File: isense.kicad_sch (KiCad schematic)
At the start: 28 parts, among them U1 MAX4073T, U2 OPA551U, U3 TLV9301xDBV, U4 OPA551U, U5 TLV9301xDBV

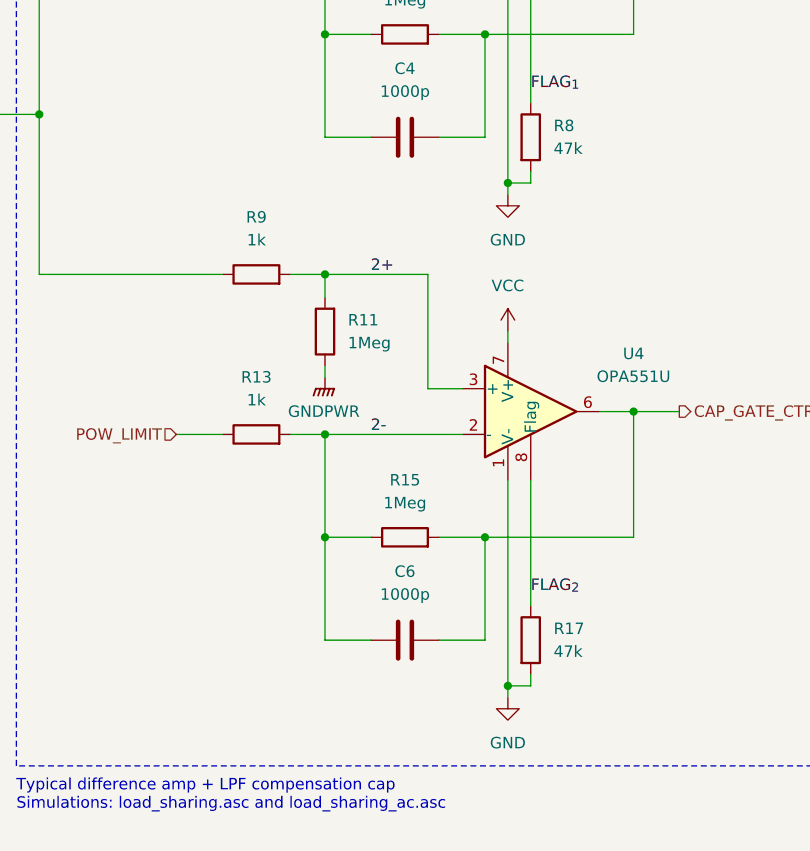
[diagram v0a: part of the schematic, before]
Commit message: Add voltage ratings to capacitors & respec caps to not explode
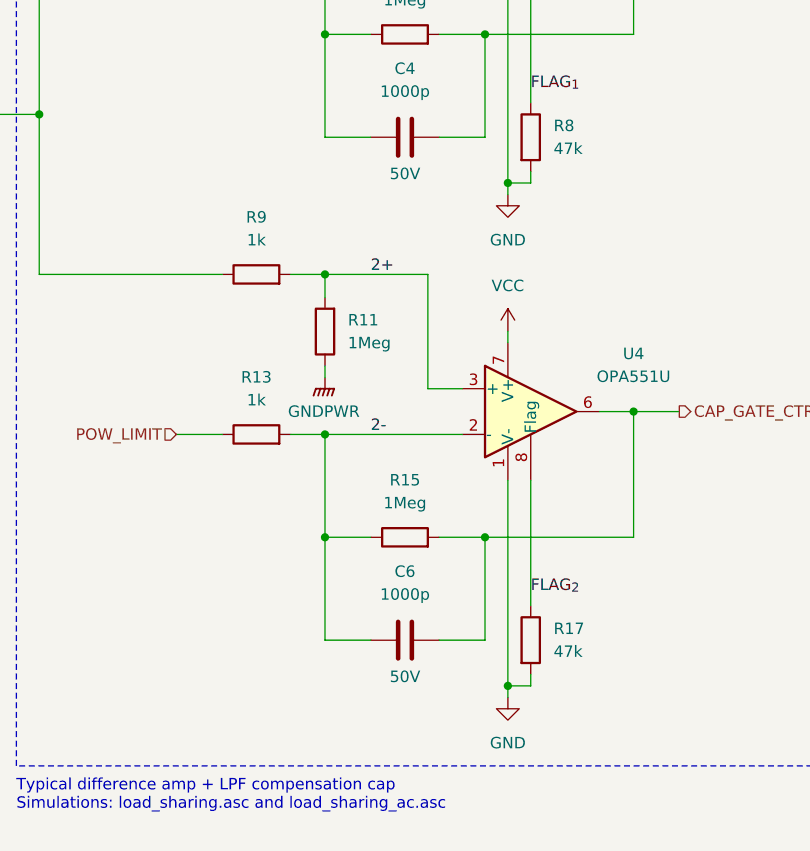
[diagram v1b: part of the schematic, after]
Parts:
- C4, C6: Voltage Rating (none) -> 50V
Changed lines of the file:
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@@
 		(on_board yes)
 		(dnp no)
-		(fields_autoplaced yes)
 		(property "Reference" "C6"
 			(at 232.41 123.19 90)
@@
 		(property "Mouser Price/Stock" ""
 			(at 232.41 130.81 0)
+			(effects
+				(font
+					(size 1.27 1.27)
+				)
+			)
+		)
+		(property "Voltage Rating" "50V"
+			(at 232.41 134.874 90)
 			(effects
 				(font
@@
 		(on_board yes)
 		(dnp no)
-		(fields_autoplaced yes)
 		(property "Reference" "C4"
 			(at 232.41 67.31 90)
@@
 			(effects
 				(font
+					(size 1.27 1.27)
+				)
+			)
+		)
+		(property "Voltage Rating" "50V"
+			(at 232.41 78.994 90)
+			(effects
+				(font

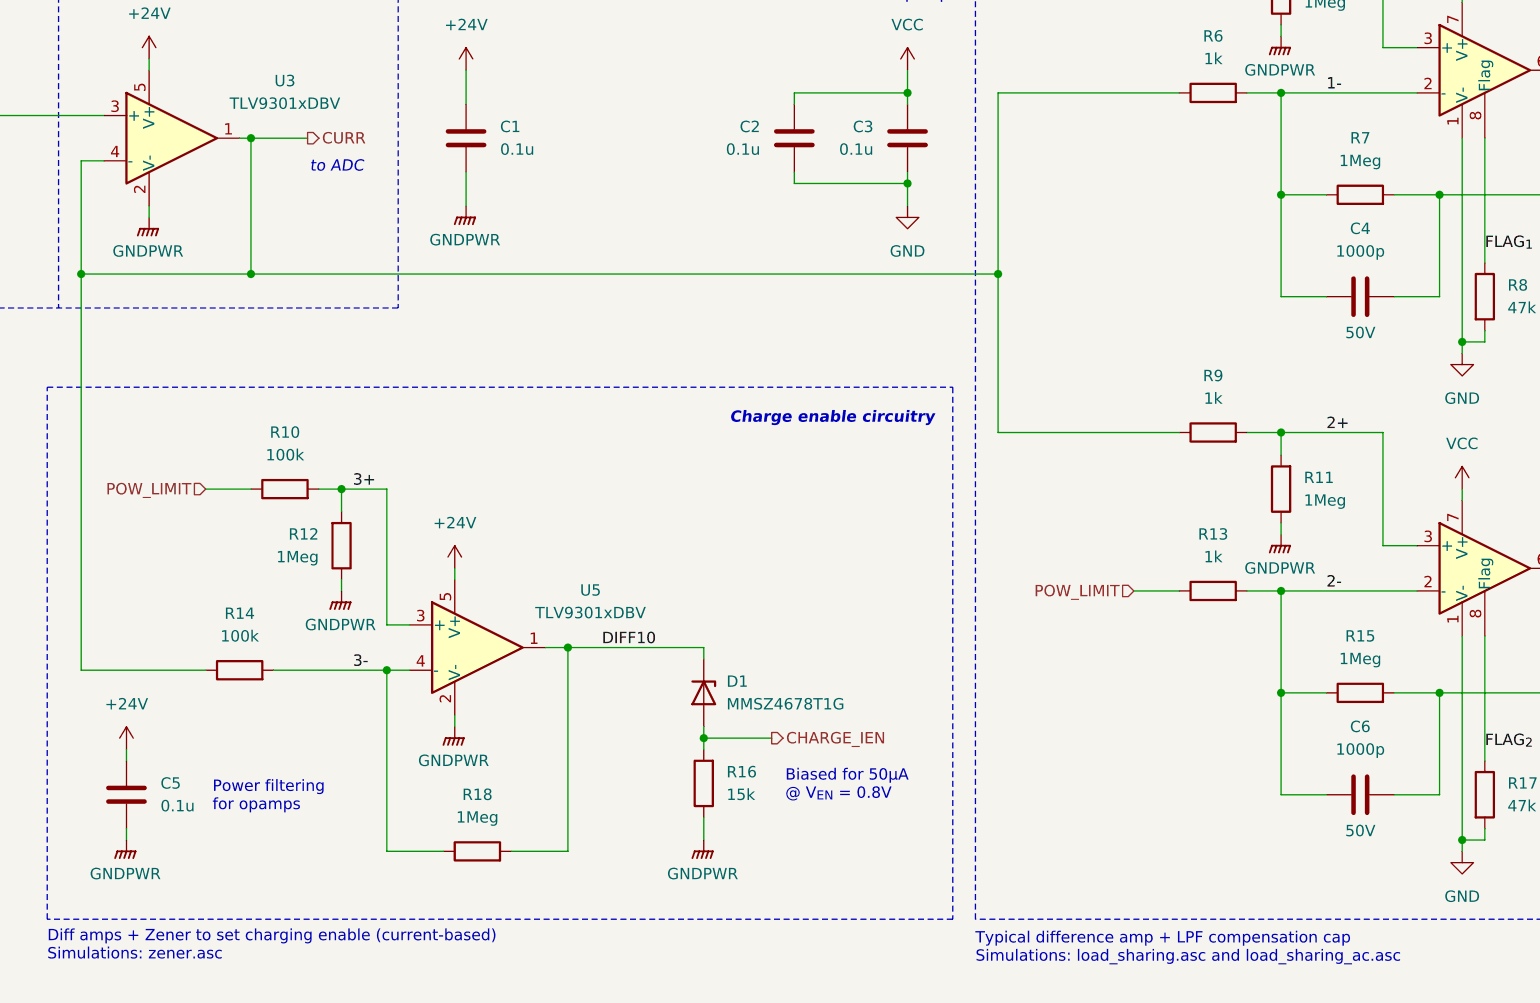
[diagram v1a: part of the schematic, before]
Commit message: Specc'd all components + started creating rev 1b boards
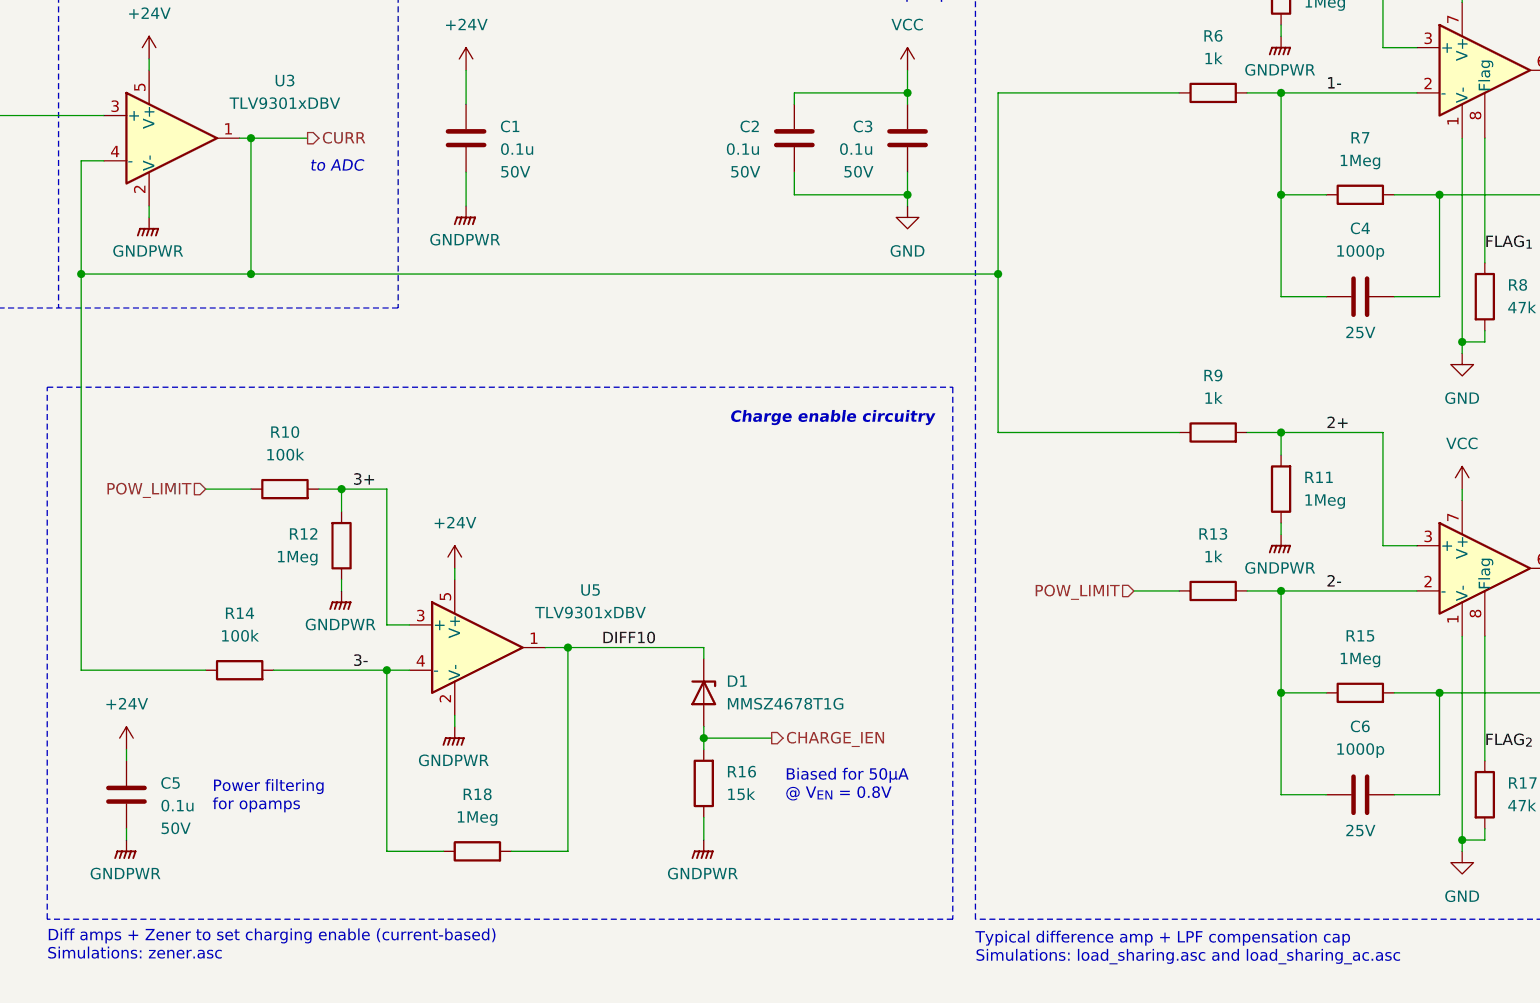
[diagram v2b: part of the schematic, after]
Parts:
- C1, C2, C3, C5: Mouser Part Number (none) -> 581-KGM15BR71H104JT; Voltage Rating (none) -> 50V
- C4, C6: Mouser Part Number 791-0603N390F500CT -> 80-C0603C102J3G; Voltage Rating 50V -> 25V
- R10, R14: Mouser Part Number (none) -> 660-RN73H1JTD1003D25
- R11, R12, R15, R18, R5, R7: Mouser Part Number 603-RC0603FR-1010ML -> 603-RC0603FR-071MP
- R13, R4, R6, R9: Mouser Part Number 755-ESR03EZPJ222 -> 660-RN73R1JTD1001F50
- R16: Mouser Part Number 603-RC0603FR-071M05L -> 603-RT0603FRE1315KL
- R17, R8: Mouser Part Number (none) -> 603-RC0603FR-1047KL
- U1: Mouser Part Number (none) -> 700-MAX4073TAUT+T
- U2, U4: Mouser Part Number (none) -> 595-OPA551UA
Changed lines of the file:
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@@
 	)
 	(junction
-		(at 181.61 62.23)
+		(at 223.52 63.5)
 		(diameter 0)
 		(color 0 0 0 0)
 	)
 	(junction
-		(at 223.52 63.5)
+		(at 181.61 63.5)
 		(diameter 0)
 		(color 0 0 0 0)
@@
 	(wire
 		(pts
-			(xy 181.61 62.23) (xy 181.61 64.77)
+			(xy 181.61 60.96) (xy 181.61 63.5)
 		)
 		(stroke
@@
 	(wire
 		(pts
-			(xy 181.61 60.96) (xy 181.61 62.23)
-		)
-		(stroke
-			(width 0)
-			(type default)
-		)
-	)
-	(wire
-		(pts
 			(xy 107.95 57.15) (xy 106.68 57.15)
 		)
@@
 	(wire
 		(pts
-			(xy 168.91 62.23) (xy 181.61 62.23)
+			(xy 181.61 63.5) (xy 181.61 64.77)
+		)
+		(stroke
+			(width 0)
+			(type default)
+		)
+	)
+	(wire
+		(pts
+			(xy 168.91 63.5) (xy 181.61 63.5)
 		)
 		(stroke
@@
 	(wire
 		(pts
-			(xy 168.91 60.96) (xy 168.91 62.23)
+			(xy 168.91 60.96) (xy 168.91 63.5)
 		)
 		(stroke
@@
 			)
 		)
-		(property "Mouser Part Number" "603-RC0603FR-1010ML"
+		(property "Mouser Part Number" "603-RC0603FR-071MP"
 			(at 223.52 40.64 0)
 			(effects
@@
 			)
 		)
-		(property "Mouser Part Number" "603-RC0603FR-071M05L"
+		(property "Mouser Part Number" "603-RT0603FRE1315KL"
 			(at 158.75 129.54 0)
 			(effects
@@
 			)
 		)
-		(property "Mouser Part Number" "603-RC0603FR-1010ML"
+		(property "Mouser Part Number" "603-RC0603FR-071MP"
 			(at 118.11 102.87 0)
 			(effects
@@
 			)
 		)
+		(property "Mouser Part Number" "660-RN73H1JTD1003D25"
+			(at 111.76 96.52 0)
+			(effects
+				(font
+					(size 1.27 1.27)
+				)
+				(hide yes)
+			)
+		)
 		(pin "1"
 		)
@@
 			)
 		)
-		(property "Mouser Part Number" "755-ESR03EZPJ222"
+		(property "Mouser Part Number" "660-RN73R1JTD1001F50"
 			(at 215.9 52.07 0)
 			(effects
@@
 			)
 		)
+		(property "Mouser Part Number" "603-RC0603FR-1047KL"
+			(at 246.38 130.81 0)
+			(effects
+				(font
+					(size 1.27 1.27)
+				)
+				(hide yes)
+			)
+		)
 		(pin "1"
 		)
@@
 			)
 		)
+		(property "Mouser Part Number" "700-MAX4073TAUT+T"
+			(at 44.45 43.18 0)
+			(effects
+				(font
+					(size 1.27 1.27)
+				)
+				(hide yes)
+			)
+		)
 		(pin "6"
 		)
@@
 		(on_board yes)
 		(dnp no)
-		(fields_autoplaced yes)
 		(property "Reference" "C2"
 			(at 165.1 55.8799 0)
@@
 			)
 		)
-		(property "Datasheet" "~"
+		(property "Datasheet" "https://www.mouser.com/datasheet/2/40/KGM_X7R-3223212.pdf"
 			(at 168.91 57.15 0)
 			(effects
@@
 			)
 		)
+		(property "Mouser Part Number" "581-KGM15BR71H104JT"
+			(at 168.91 57.15 0)
+			(effects
+				(font
+					(size 1.27 1.27)
+				)
+				(hide yes)
+			)
+		)
+		(property "Voltage Rating" "50V"
+			(at 165.1 60.96 0)
+			(effects
+				(font
+					(size 1.27 1.27)
+				)
+				(justify left)
+			)
+		)
 		(pin "2"
 		)
@@
 			)
 		)
+		(property "Mouser Part Number" "595-OPA551UA"
+			(at 246.38 49.53 0)
+			(effects
+				(font
+					(size 1.27 1.27)
+				)
+				(hide yes)
+			)
+		)
 		(pin "1"
 		)
@@
 			)
 		)
-		(property "Mouser Part Number" "755-ESR03EZPJ222"
+		(property "Mouser Part Number" "660-RN73R1JTD1001F50"
 			(at 215.9 107.95 0)
 			(effects
@@
 			)
 		)
+		(property "Mouser Part Number" "603-RC0603FR-1047KL"
+			(at 246.38 74.93 0)
+			(effects
+				(font
+					(size 1.27 1.27)
+				)
+				(hide yes)
+			)
+		)
 		(pin "1"
 		)
@@
 			)
 		)
+		(property "Mouser Part Number" "595-OPA551UA"
+			(at 246.38 105.41 0)
+			(effects
+				(font
+					(size 1.27 1.27)
+				)
+				(hide yes)
+			)
+		)
 		(pin "1"
 		)
@@
 			)
 		)
-		(property "Mouser Part Number" "603-RC0603FR-1010ML"
+		(property "Mouser Part Number" "603-RC0603FR-071MP"
 			(at 232.41 63.5 0)
 			(effects
@@
 			)
 		)
-		(property "Mouser Part Number" "603-RC0603FR-1010ML"
+		(property "Mouser Part Number" "603-RC0603FR-071MP"
 			(at 133.35 137.16 0)
 			(effects
@@
 			)
 		)
-		(property "Mouser Part Number" "791-0603N390F500CT"
+		(property "Mouser Part Number" "80-C0603C102J3G"
 			(at 232.41 130.81 90)
 			(effects
@@
 			)
 		)
-		(property "Voltage Rating" "50V"
+		(property "Voltage Rating" "25V"
 			(at 232.41 134.874 90)
 			(effects
@@
 		(on_board yes)
 		(dnp no)
-		(fields_autoplaced yes)
 		(property "Reference" "C5"
 			(at 97.79 129.5399 0)
@@
 			)
 		)
-		(property "Datasheet" "~"
+		(property "Datasheet" "https://www.mouser.com/datasheet/2/40/KGM_X7R-3223212.pdf"
 			(at 93.98 130.81 0)
 			(effects
@@
 			)
 		)
+		(property "Mouser Part Number" "581-KGM15BR71H104JT"
+			(at 93.98 130.81 0)
+			(effects
+				(font
+					(size 1.27 1.27)
+				)
+				(hide yes)
+			)
+		)
+		(property "Voltage Rating" "50V"
+			(at 97.79 134.62 0)
+			(effects
+				(font
+					(size 1.27 1.27)
+				)
+				(justify left)
+			)
+		)
 		(pin "2"
 		)
@@
 			)
 		)
-		(property "Mouser Part Number" "755-ESR03EZPJ222"
+		(property "Mouser Part Number" "660-RN73R1JTD1001F50"
 			(at 215.9 90.17 0)
 			(effects
@@
 			)
 		)
-		(property "Mouser Part Number" "603-RC0603FR-1010ML"
+		(property "Mouser Part Number" "603-RC0603FR-071MP"
 			(at 232.41 119.38 0)
 			(effects
@@
 		(on_board yes)
 		(dnp no)
-		(fields_autoplaced yes)
 		(property "Reference" "C3"
 			(at 177.8 55.8799 0)
@@
 			)
 		)
-		(property "Datasheet" "~"
+		(property "Datasheet" "https://www.mouser.com/datasheet/2/40/KGM_X7R-3223212.pdf"
 			(at 181.61 57.15 0)
 			(effects
@@
 			)
 		)
+		(property "Mouser Part Number" "581-KGM15BR71H104JT"
+			(at 181.61 57.15 0)
+			(effects
+				(font
+					(size 1.27 1.27)
+				)
+				(hide yes)
+			)
+		)
+		(property "Voltage Rating" "50V"
+			(at 177.8 60.96 0)
+			(effects
+				(font
+					(size 1.27 1.27)
+				)
+				(justify left)
+			)
+		)
 		(pin "2"
 		)
@@
 			)
 		)
-		(property "Mouser Part Number" "755-ESR03EZPJ222"
+		(property "Mouser Part Number" "660-RN73R1JTD1001F50"
 			(at 215.9 34.29 0)
 			(effects
@@
 		(on_board yes)
 		(dnp no)
-		(fields_autoplaced yes)
 		(property "Reference" "C1"
 			(at 135.89 55.8799 0)
@@
 			)
 		)
-		(property "Datasheet" "~"
+		(property "Datasheet" "https://www.mouser.com/datasheet/2/40/KGM_X7R-3223212.pdf"
 			(at 132.08 57.15 0)
 			(effects
@@
 			)
 		)
+		(property "Mouser Part Number" "581-KGM15BR71H104JT"
+			(at 132.08 57.15 0)
+			(effects
+				(font
+					(size 1.27 1.27)
+				)
+				(hide yes)
+			)
+		)
+		(property "Voltage Rating" "50V"
+			(at 135.89 60.96 0)
+			(effects
+				(font
+					(size 1.27 1.27)
+				)
+				(justify left)
+			)
+		)
 		(pin "2"
 		)
@@
 			)
 		)
+		(property "Mouser Part Number" "660-RN73H1JTD1003D25"
+			(at 106.68 116.84 0)
+			(effects
+				(font
+					(size 1.27 1.27)
+				)
+				(hide yes)
+			)
+		)
 		(pin "1"
 		)
@@
 			)
 		)
-		(property "Mouser Part Number" "603-RC0603FR-1010ML"
+		(property "Mouser Part Number" "603-RC0603FR-071MP"
 			(at 223.52 96.52 0)
 			(effects
@@
 			)
 		)
-		(property "Mouser Part Number" "791-0603N390F500CT"
+		(property "Mouser Part Number" "80-C0603C102J3G"
 			(at 232.41 74.93 90)
 			(effects
@@
 			)
 		)
-		(property "Voltage Rating" "50V"
+		(property "Voltage Rating" "25V"
 			(at 232.41 78.994 90)
 			(effects

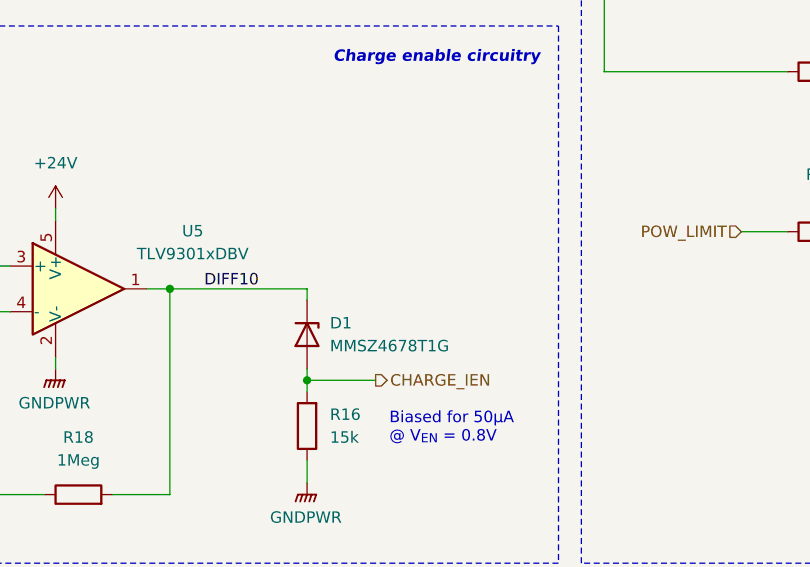
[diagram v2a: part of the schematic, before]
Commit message: Add test points to all subsheets
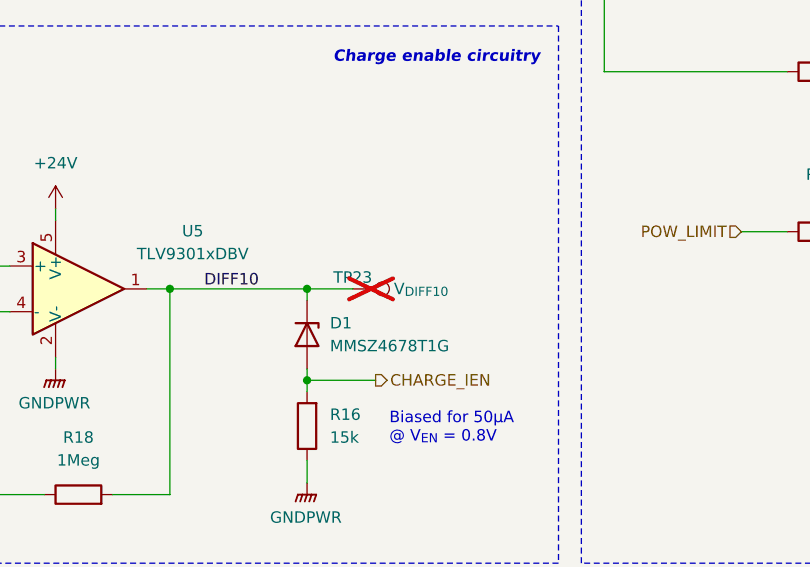
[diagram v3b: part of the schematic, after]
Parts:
- added TP23: V_{DIFF10}, TestPoint:TestPoint_Bridge_Pitch2.0mm_Drill0.7mm, symbol Connector:TestPoint
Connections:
- net DIFF10: now also TP23.1

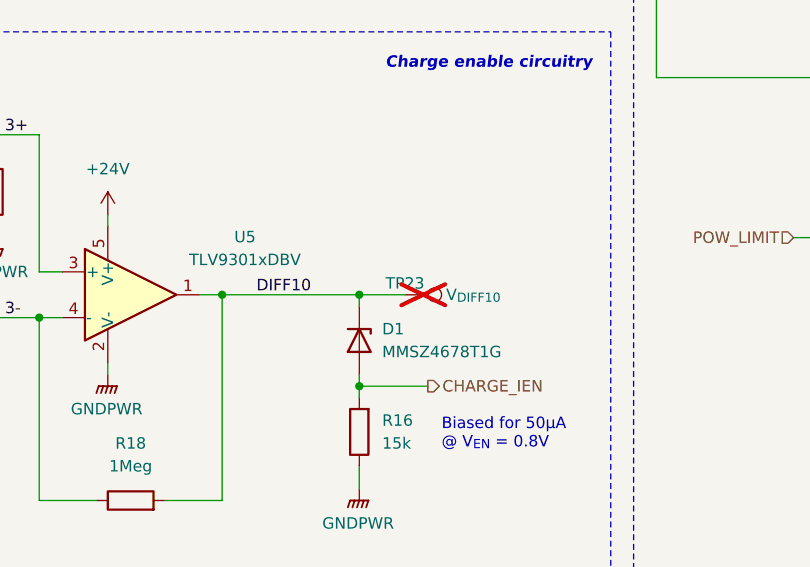
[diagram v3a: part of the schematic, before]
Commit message: Renumbered components for rev 1b layout
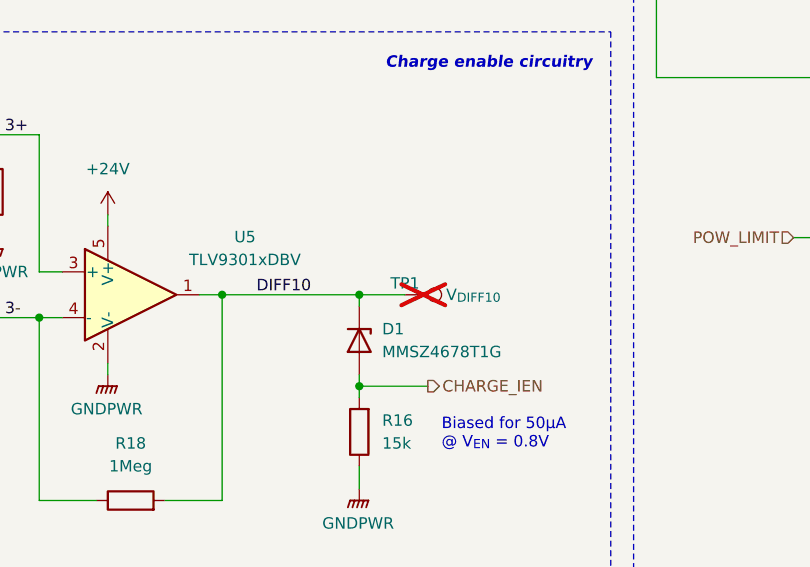
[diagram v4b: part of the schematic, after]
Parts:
- renumbered TP23 to TP1
